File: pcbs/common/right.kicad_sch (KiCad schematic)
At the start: 89 parts, among them J2 TRS

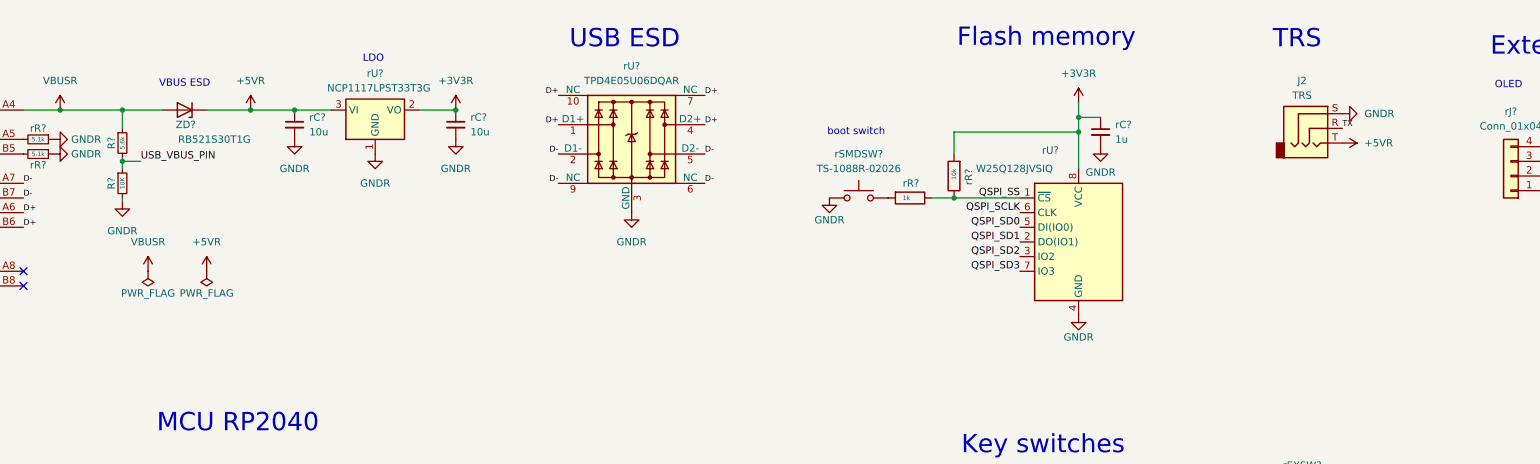
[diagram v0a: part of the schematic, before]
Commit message: Add USB C port to replace TRS jack
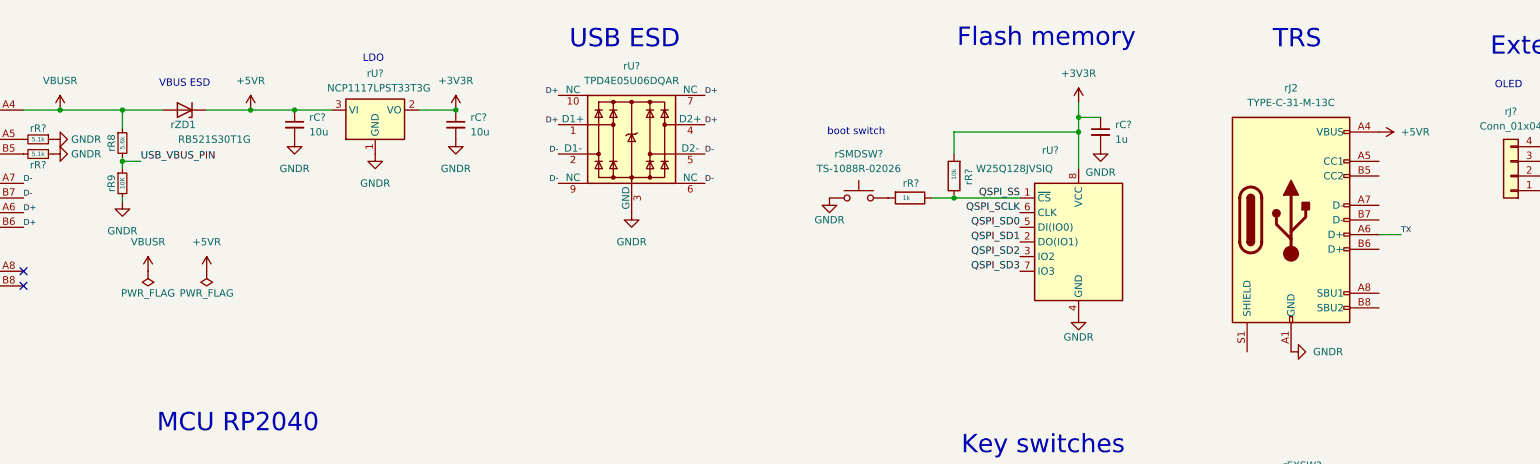
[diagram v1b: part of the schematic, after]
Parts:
- removed J2: TRS, kbd_local:PJ-398A-5A_PJ-399B-6A, symbol Connector_Audio:AudioJack3
- added rJ2: TYPE-C-31-M-13C, kbd:TYPE-C-31-M-13C, symbol Connector:USB_C_Receptacle_USB2.0
- gave numbers to parts that had none: 3
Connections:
- net +5VR: now also rJ2.A4 (VBUS), rJ2.A9 (VBUS), rJ2.B4 (VBUS), rJ2.B9 (VBUS)
- net GNDR: now also rJ2.A1 (GND), rJ2.A12 (GND), rJ2.B1 (GND), rJ2.B12 (GND)
- net TX: now also rJ2.A6 (D+)

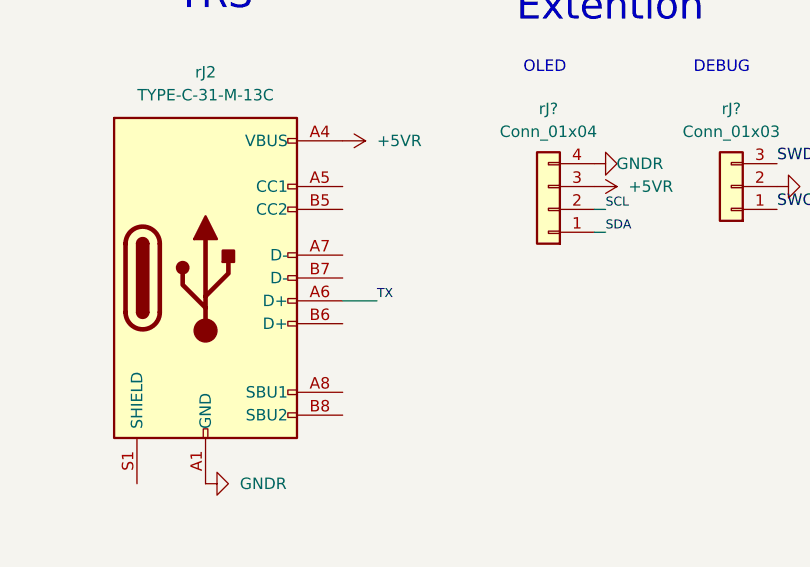
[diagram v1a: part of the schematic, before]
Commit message: Fix some connections
Also connect the other USB D+ pin to the controller.
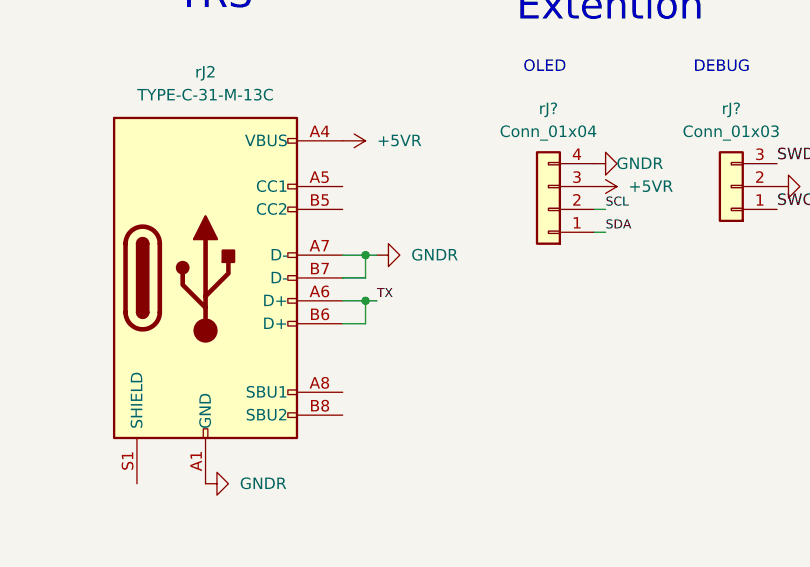
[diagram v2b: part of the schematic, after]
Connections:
- net GNDR: now also rJ2.A7 (D-), rJ2.B7 (D-)
- net TX: now also rJ2.B6 (D+)
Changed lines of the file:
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@@
 	)
 	(junction
+		(at 283.21 54.61)
+		(diameter 0)
+		(color 0 0 0 0)
+	)
+	(junction
 		(at 271.78 262.89)
 		(diameter 0)
@@
 	)
 	(junction
+		(at 283.21 49.53)
+		(diameter 0)
+		(color 0 0 0 0)
+	)
+	(junction
 		(at 256.54 262.89)
 		(diameter 0)
@@
 	(wire
 		(pts
+			(xy 283.21 57.15) (xy 283.21 54.61)
+		)
+		(stroke
+			(width 0)
+			(type default)
+		)
+	)
+	(wire
+		(pts
+			(xy 283.21 52.07) (xy 283.21 49.53)
+		)
+		(stroke
+			(width 0)
+			(type default)
+		)
+	)
+	(wire
+		(pts
+			(xy 280.67 52.07) (xy 283.21 52.07)
+		)
+		(stroke
+			(width 0)
+			(type default)
+		)
+	)
+	(wire
+		(pts
 			(xy 86.36 114.3) (xy 86.36 120.65)
 		)
@@
 	(wire
 		(pts
-			(xy 280.67 54.61) (xy 284.48 54.61)
+			(xy 280.67 54.61) (xy 283.21 54.61)
 		)
 		(stroke
@@
 	(wire
 		(pts
+			(xy 280.67 49.53) (xy 283.21 49.53)
+		)
+		(stroke
+			(width 0)
+			(type default)
+		)
+	)
+	(wire
+		(pts
 			(xy 287.02 208.28) (xy 287.02 227.33)
 		)
@@
 	(wire
 		(pts
+			(xy 283.21 49.53) (xy 284.48 49.53)
+		)
+		(stroke
+			(width 0)
+			(type default)
+		)
+	)
+	(wire
+		(pts
 			(xy 241.3 227.33) (xy 241.3 245.11)
 		)
@@
 	(wire
 		(pts
+			(xy 280.67 57.15) (xy 283.21 57.15)
+		)
+		(stroke
+			(width 0)
+			(type default)
+		)
+	)
+	(wire
+		(pts
 			(xy 264.16 215.9) (xy 264.16 219.71)
 		)
@@
 	(wire
 		(pts
+			(xy 283.21 54.61) (xy 284.48 54.61)
+		)
+		(stroke
+			(width 0)
+			(type default)
+		)
+	)
+	(wire
+		(pts
 			(xy 226.06 190.5) (xy 226.06 208.28)
 		)
@@
 					(unit 1)
 				)
+			)
+		)
+	)
+	(symbol
+		(lib_id "kbd:GNDR")
+		(at 284.48 49.53 90)
+		(unit 1)
+		(exclude_from_sim no)
+		(in_bom yes)
+		(on_board yes)
+		(dnp no)
+		(property "Reference" "#PWR57"
+			(at 290.83 49.53 0)
+			(effects
+				(font
+					(size 1.27 1.27)
+				)
+				(hide yes)
+			)
+		)
+		(property "Value" "GNDR"
+			(at 288.29 49.53 90)
+			(effects
+				(font
+					(size 1.27 1.27)
+				)
+				(justify right)
+			)
+		)
+		(property "Footprint" ""
+			(at 284.48 49.53 0)
+			(effects
+				(font
+					(size 1.27 1.27)
+				)
+				(hide yes)
+			)
+		)
+		(property "Datasheet" ""
+			(at 284.48 49.53 0)
+			(effects
+				(font
+					(size 1.27 1.27)
+				)
+				(hide yes)
+			)
+		)
+		(property "Description" ""
+			(at 284.48 49.53 0)
+			(effects
+				(font
+					(size 1.27 1.27)
+				)
+				(hide yes)
+			)
+		)
+		(pin "1"
+		)
+		(instances
+			(project "corne-cherry"
+				(path "/4cc5d416-57f5-4147-8183-e03ae6b1198a/50d96a5e-3d25-4129-9495-15388c76587f"
+					(reference "#PWR57")
+					(unit 1)
+				)
